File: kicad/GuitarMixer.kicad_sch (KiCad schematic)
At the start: 49 parts, among them J1 Conn_01x03_Pin, J2 Conn_01x03_Pin, J3 Conn_01x03_Pin, J4 Conn_01x02_Pin, J5 Conn_01x02_Pin, J6 Conn_01x03_Pin, Q1 2N5457, SW1 SW_SPST, U1 TL072, U2 TL072

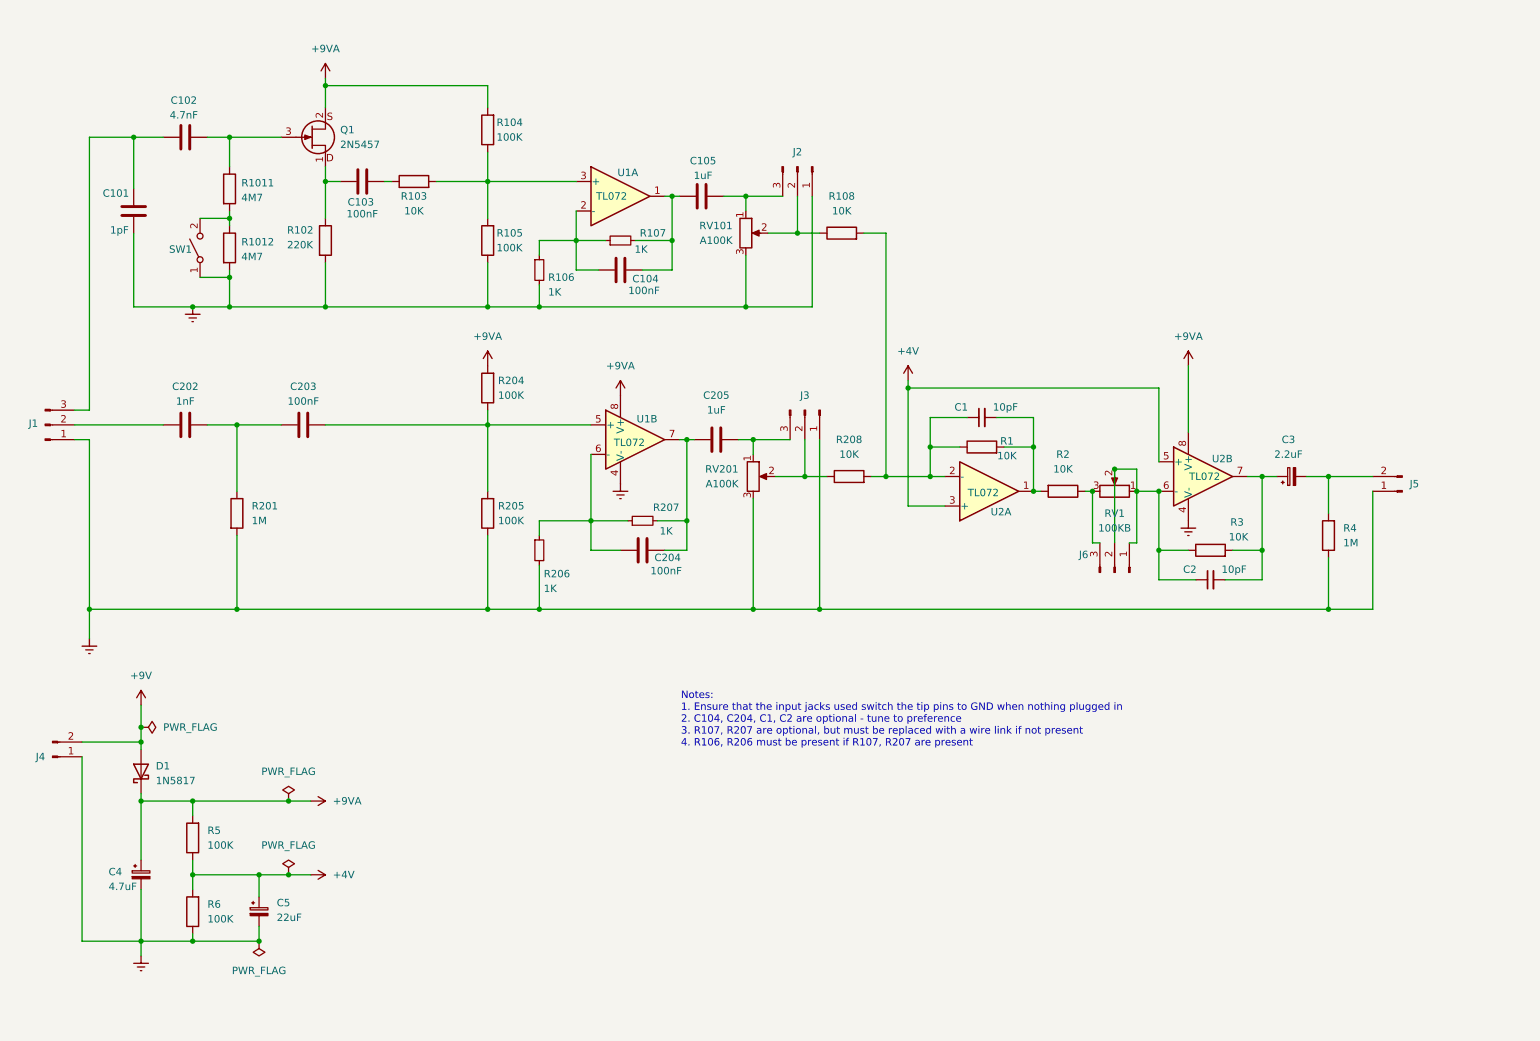
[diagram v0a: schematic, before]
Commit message: New version with split rail power supply
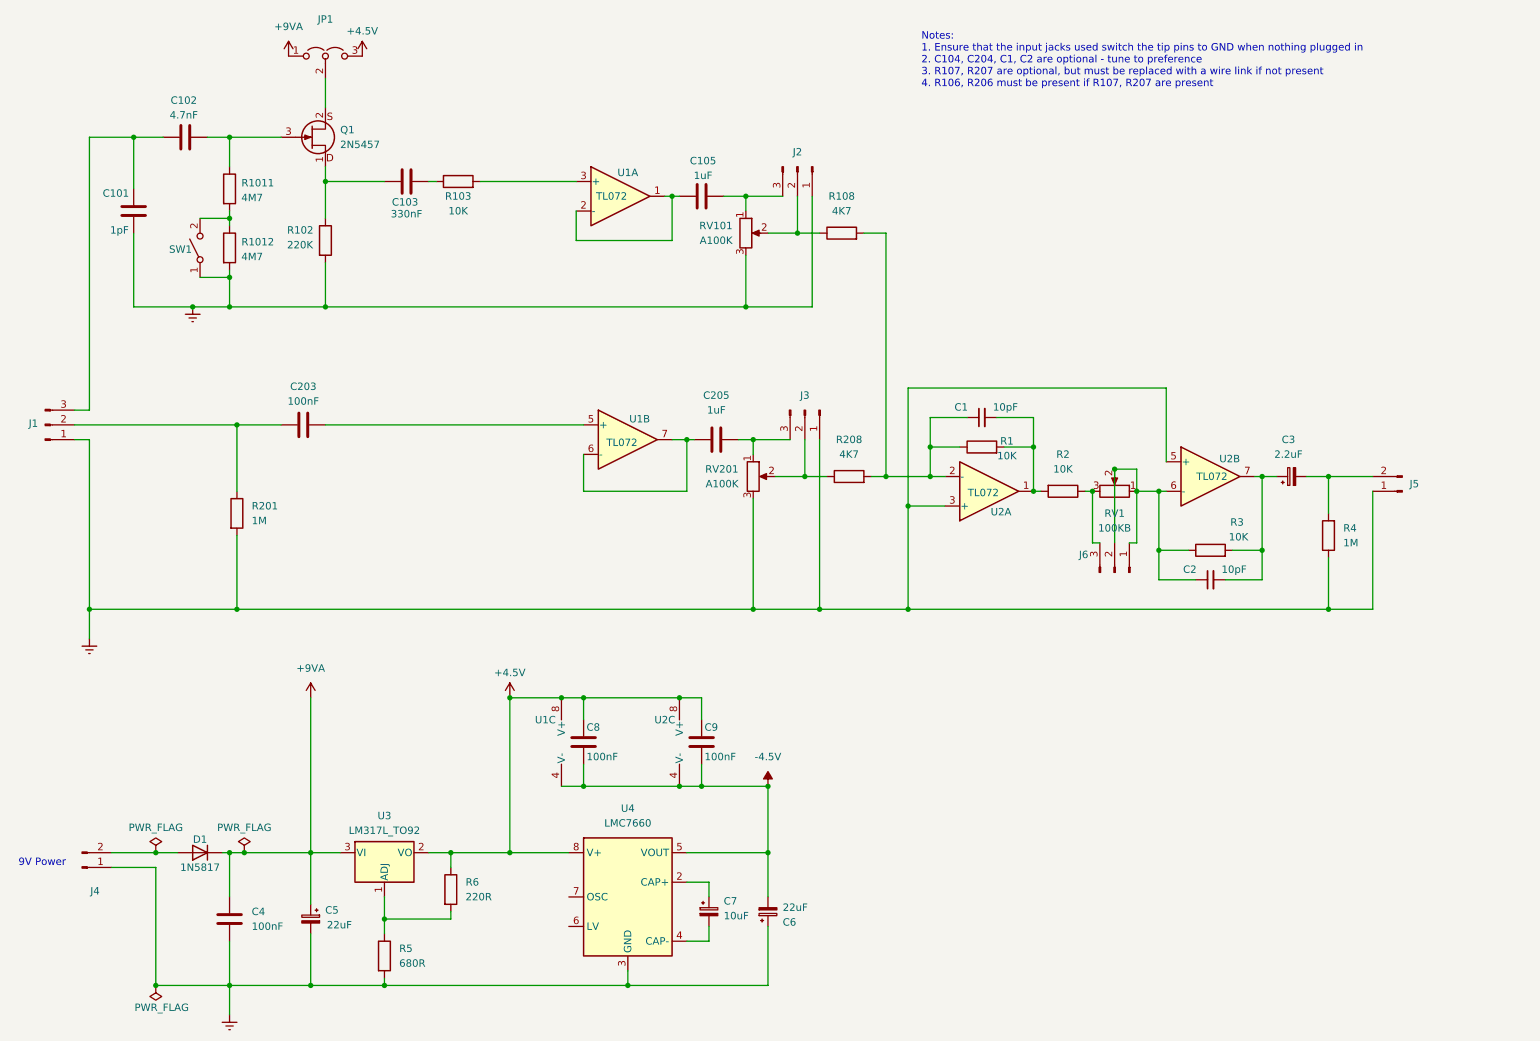
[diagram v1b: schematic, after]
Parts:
- removed C104, C204: 100nF, Capacitor_THT:C_Rect_L7.2mm_W2.5mm_P5.00mm_FKS2_FKP2_MKS2_MKP2, symbol Device:C
- removed C202: 1nF, Capacitor_THT:C_Rect_L7.2mm_W2.5mm_P5.00mm_FKS2_FKP2_MKS2_MKP2, symbol Device:C
- removed C4: 4.7uF, Capacitor_THT:CP_Radial_D5.0mm_P2.00mm, symbol Device:C_Polarized_Small
- removed D1: 1N5817, Diode_THT:D_DO-41_SOD81_P10.16mm_Horizontal, symbol Diode:1N5817
- removed R104, R105, R204, R205: 100K, Resistor_THT:R_Axial_DIN0207_L6.3mm_D2.5mm_P10.16mm_Horizontal, symbol Device:R
- removed R106, R107, R206, R207: 1K, Resistor_THT:R_Axial_DIN0207_L6.3mm_D2.5mm_P10.16mm_Horizontal, symbol Device:R_Small
- added C4, C8, C9: 100nF, Capacitor_THT:C_Rect_L7.0mm_W3.5mm_P5.00mm, symbol Device:C
- added C6: 22uF, Capacitor_THT:CP_Radial_D5.0mm_P2.00mm, symbol Device:C_Polarized_Small
- added C7: 10uF, Capacitor_THT:CP_Radial_D5.0mm_P2.00mm, symbol Device:C_Polarized_Small
- added D1: 1N5817, Diode_THT:D_DO-35_SOD27_P2.54mm_Vertical_AnodeUp, symbol Diode:1N4007
- added JP1: Jumper_3_Open, Jumper:SolderJumper-3_P1.3mm_Open_Pad1.0x1.5mm, symbol Jumper:Jumper_3_Open
- added U3: LM317L_TO92, Package_TO_SOT_THT:TO-92_HandSolder, symbol Regulator_Linear:LM317L_TO92
- added U4: LMC7660, Package_DIP:DIP-8_W7.62mm, symbol Regulator_SwitchedCapacitor:LMC7660
- C103: value 100nF -> 330nF
- R108, R208: value 10K -> 4K7; footprint Resistor_THT:R_Axial_DIN0207_L6.3mm_D2.5mm_P10.16mm_Horizontal -> Resistor_THT:R_Axial_DIN0207_L6.3mm_D2.5mm_P2.54mm_Vertical
- R5: value 100K -> 680R; footprint Resistor_THT:R_Axial_DIN0207_L6.3mm_D2.5mm_P10.16mm_Horizontal -> Resistor_THT:R_Axial_DIN0207_L6.3mm_D2.5mm_P2.54mm_Vertical
- R6: value 100K -> 220R; footprint Resistor_THT:R_Axial_DIN0207_L6.3mm_D2.5mm_P10.16mm_Horizontal -> Resistor_THT:R_Axial_DIN0207_L6.3mm_D2.5mm_P2.54mm_Vertical
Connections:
- net +9VA: now also C5.1, C4.1, D1.1 (K), JP1.1 (A), U3.3 (VI); no longer Q1.2 (D), R5.2, U1.8 (V+), U2.8 (V+)
- net Earth: now also R5.2, U2.3 (+), U2.5 (+), C4.2, C6.1, U4.3 (GND); no longer R6.1, U1.4 (V-), U2.4 (V-)
- net at J1.2 (Pin_2): now also C203.1, R201.1
- net at U1.2 (-): now also C105.1, U1.1
- net at U1.6 (-): now also C205.1, U1.7
- removed net +4V: C5.1, R5.1, R6.2, U2.3 (+), U2.5 (+)
- net +9V: no longer names the net of J4.2 (Pin_2)
- net +9V: now also D1.2 (A)
- new net: C7.1, U4.2 (CAP+)
- new net: C7.2, U4.4 (CAP-)
- new net: R5.1, R6.2, U3.1 (ADJ)
- new net: JP1.2 (C), Q1.2 (D)
- new net +4.5V: C8.1, C9.1, JP1.3 (B), R6.1, U1.8 (V+), U2.8 (V+), U3.2 (VO), U4.8 (V+)
- new net -4.5V: C6.2, C8.2, C9.2, U1.4 (V-), U2.4 (V-), U4.5 (VOUT)
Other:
- note added: "9V Power"
- moved on the sheet: C103, R103, U1B, U2B

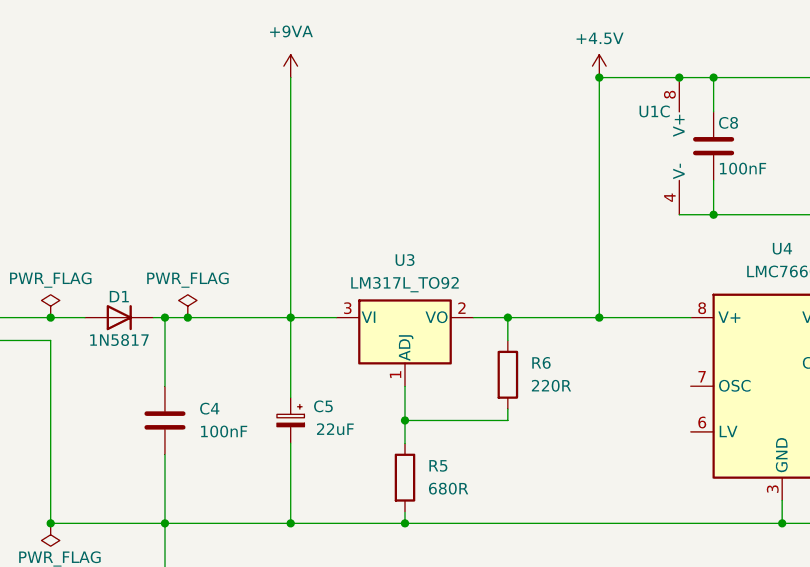
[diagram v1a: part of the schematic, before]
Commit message: Moved the voltage setting resistors and created gerber and distribution files
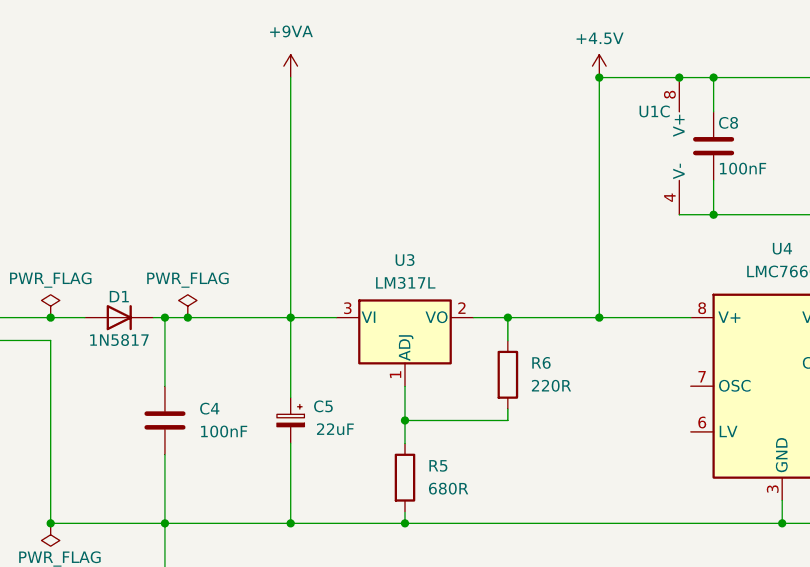
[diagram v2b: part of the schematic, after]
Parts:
- D1: footprint Diode_THT:D_DO-35_SOD27_P2.54mm_Vertical_AnodeUp -> Diode_THT:D_DO-35_SOD27_P7.62mm_Horizontal
- U3: value LM317L_TO92 -> LM317L
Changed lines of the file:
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@@
 			)
 		)
-		(property "Footprint" "Diode_THT:D_DO-35_SOD27_P2.54mm_Vertical_AnodeUp"
+		(property "Footprint" "Diode_THT:D_DO-35_SOD27_P7.62mm_Horizontal"
 			(at 57.15 158.115 0)
 			(effects
@@
 			)
 		)
-		(property "Datasheet" "http://www.vishay.com/docs/88503/1n4001.pdf"
+		(property "Datasheet" ""
 			(at 57.15 162.56 0)
 			(effects
@@
 			)
 		)
-		(property "Description" "1000V 1A General Purpose Rectifier Diode, DO-41"
+		(property "Description" ""
 			(at 57.15 162.56 0)
 			(effects
@@
 			)
 		)
-		(property "Value" "LM317L_TO92"
+		(property "Value" "LM317L"
 			(at 88.9 158.75 0)
 			(effects
